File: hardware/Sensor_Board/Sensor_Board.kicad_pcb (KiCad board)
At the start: 4 copper layers, 83 x 83 mm, 67 parts, among them J1 Antenna, J2 Antenna, J3 Sensors, U1 ICM-42670-P, U10 PE42421, U12 SX1262IMLTRT, U2 SX1262IMLTRT, U3 0900FM15D0039, U4 BME280, U5 PE42421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

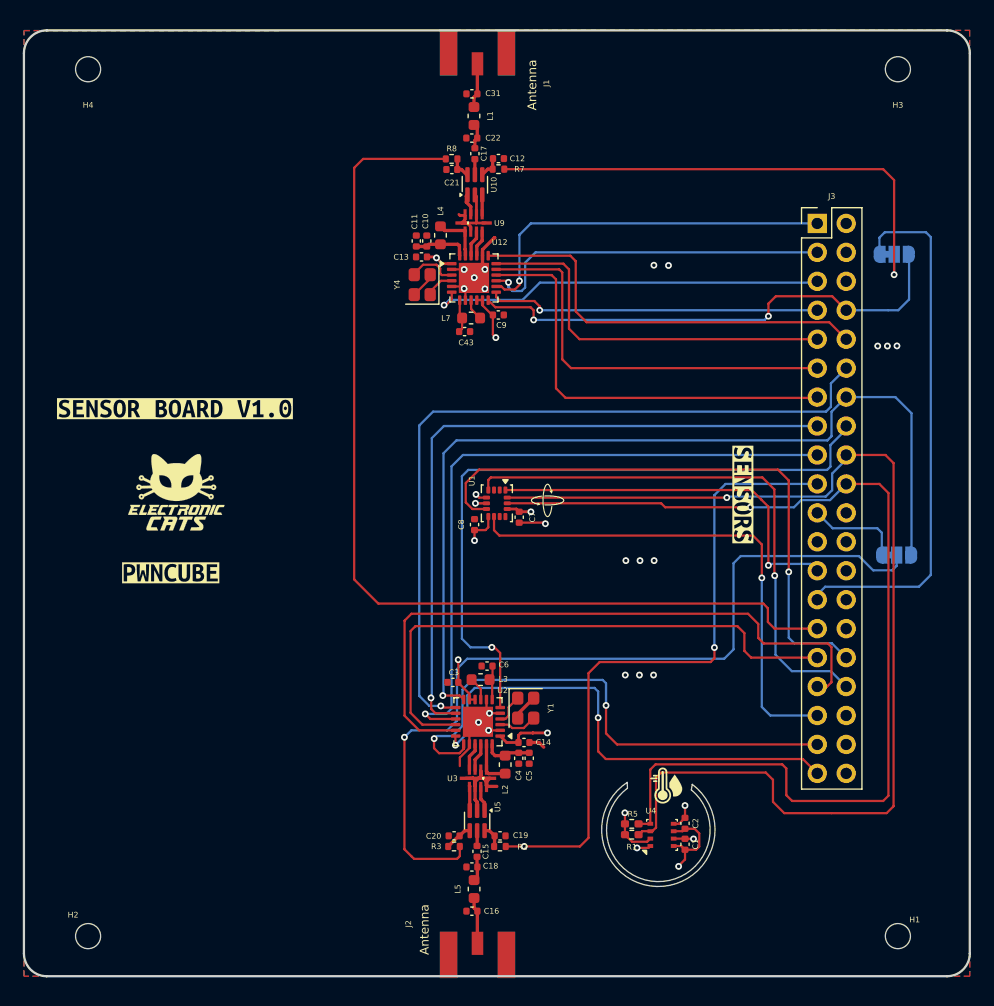
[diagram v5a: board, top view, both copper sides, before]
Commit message: feat(Hw):labels_updated
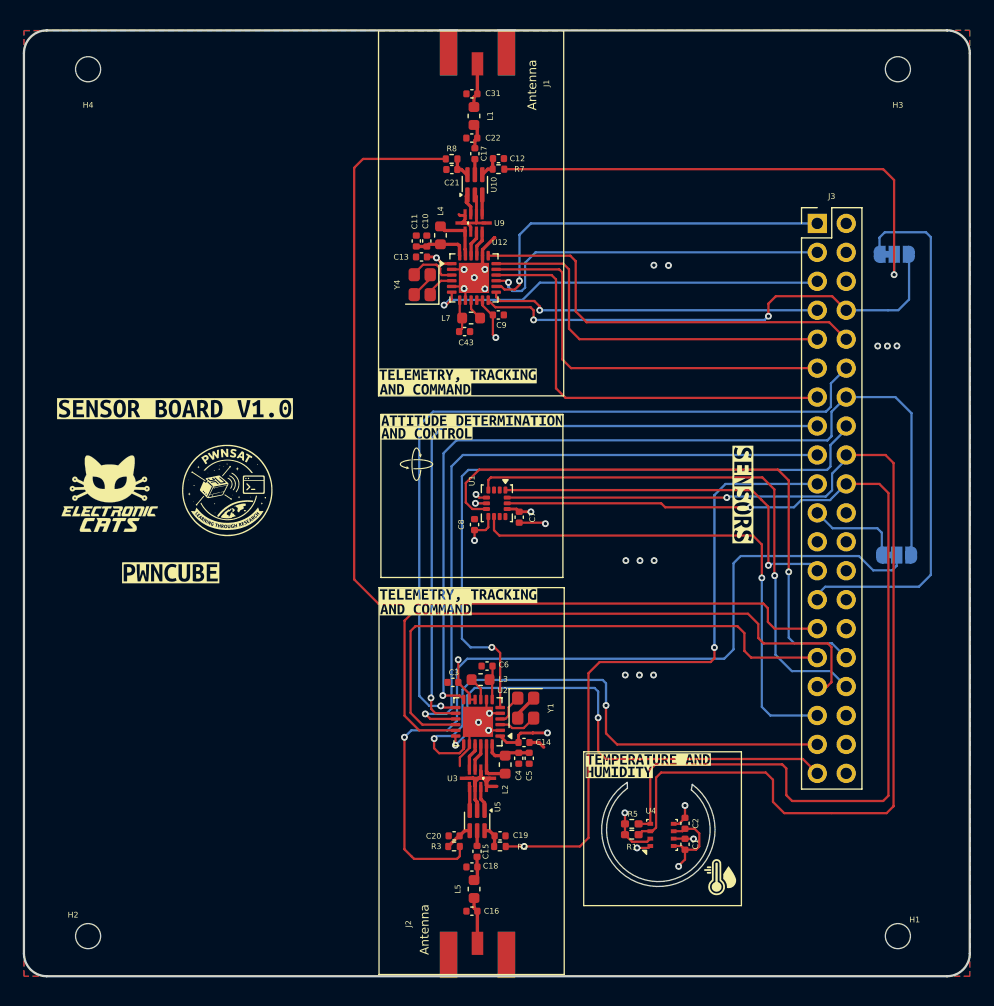
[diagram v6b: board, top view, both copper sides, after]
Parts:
- added kibuzzard-698668F8: G***, kibuzzard-698668F8, F.Cu at (124.6, 122.6)
- added kibuzzard-69866904: G***, kibuzzard-69866904, F.Cu at (122.0, 123.7)
- added kibuzzard-698669D4: G***, kibuzzard-698669D4, F.Cu at (107.9, 108.3)
- added kibuzzard-698669D4: G***, kibuzzard-698669D4, F.Cu at (107.9, 89.0)
- added kibuzzard-698669E3: G***, kibuzzard-698669E3, F.Cu at (105.0, 109.4)
- added kibuzzard-698669E3: G***, kibuzzard-698669E3, F.Cu at (105.0, 90.2)
- added kibuzzard-69866AEC: G***, kibuzzard-69866AEC, F.Cu at (109.1, 92.9)
- added kibuzzard-69866B09: G***, kibuzzard-69866B09, F.Cu at (105.1, 94.0)
- moved G*** 11.9 mm to (104.2, 96.7)
- moved G*** 9.33 mm to (130.9, 133.0)
- moved G*** 5.84 mm to (77.3, 99.3)

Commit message: feat(Hw):BoM´s_Updated
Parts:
- C10, C13, C14, C3, C4, C9: value 0.1uF -> 100nF
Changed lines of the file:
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@@
 				(font
 					(size 0.001 0.001)
+					(thickness 0.15)
 				)
 			)
@@
 				(font
 					(size 0.001 0.001)
+					(thickness 0.15)
 				)
 			)
@@
 				(font
 					(size 0.001 0.001)
+					(thickness 0.15)
 				)
 			)
@@
 				(font
 					(size 0.001 0.001)
+					(thickness 0.15)
 				)
 			)
@@
 			)
 		)
+		(property "LCSC#" "C170151"
+			(at 0 0 90)
+			(unlocked yes)
+			(layer "F.Fab")
+			(hide yes)
+			(effects
+				(font
+					(size 1 1)
+					(thickness 0.15)
+				)
+			)
+		)
 		(property ki_fp_filters "C_*")
 		(sheetname "/Sensors/")
@@
 			)
 		)
-		(property "LCSC#" "C710873 "
+		(property "LCSC#" "C76947"
 			(at 0 0 180)
 			(unlocked yes)
@@
 			)
 		)
-		(property "LCSC#" "C710873 "
+		(property "LCSC#" "C76947"
 			(at 0 0 0)
 			(unlocked yes)
@@
 			)
 		)
-		(property "Value" "0.1uF"
+		(property "Value" "100nF"
 			(at 0 1.16 0)
 			(layer "F.Fab")
@@
 			)
 		)
-		(property "Value" "0.1uF"
+		(property "Value" "100nF"
 			(at 0 1.16 90)
 			(layer "F.Fab")
@@
 			)
 		)
-		(property "Value" "0.1uF"
+		(property "Value" "100nF"
 			(at 0 1.16 90)
 			(layer "F.Fab")
@@
 				(font
 					(size 0.001 0.001)
+					(thickness 0.15)
 				)
 			)
@@
 				(font
 					(size 0.001 0.001)
+					(thickness 0.15)
 				)
 			)
@@
 				(font
 					(size 0.001 0.001)
+					(thickness 0.15)
 				)
 			)
@@
 				(font
 					(size 0.001 0.001)
+					(thickness 0.15)
 				)
 			)
@@
 			)
 		)
-		(property "Datasheet" "https://datasheet.lcsc.com/lcsc/2110081230_Sunlord-SDFL1608T150KTF_C57838.pdf"
+		(property "Datasheet" "https://www.lcsc.com/datasheet/C2885870.pdf"
 			(at 0 0 0)
 			(layer "F.Fab")
@@
 			)
 		)
-		(property "LCSC#" "C57838"
+		(property "LCSC#" "C2885870"
 			(at 0 0 180)
 			(unlocked yes)
@@
 			)
 		)
+		(property "LCSC#" "C7501249"
+			(at 0 0 0)
+			(unlocked yes)
+			(layer "F.Fab")
+			(hide yes)
+			(effects
+				(font
+					(size 1 1)
+					(thickness 0.15)
+				)
+			)
+		)
 		(property ki_fp_filters "Connector*:*_2x??_*")
 		(sheetname "/Inputs_Connectors/")
@@
 			)
 		)
-		(property "LCSC#" "C710873 "
+		(property "LCSC#" "C76947"
 			(at 0 0 0)
 			(unlocked yes)
@@
 			)
 		)
-		(property "Value" "0.1uF"
+		(property "Value" "100nF"
 			(at 0 1.16 0)
 			(layer "F.Fab")
@@
 			)
 		)
-		(property "Datasheet" "~"
+		(property "Datasheet" ""
 			(at 0 0 90)
 			(layer "F.Fab")
@@
 			)
 		)
-		(property "Datasheet" "~"
+		(property "Datasheet" ""
 			(at 0 0 90)
 			(layer "F.Fab")
@@
 				(font
 					(size 0.001 0.001)
+					(thickness 0.15)
 				)
 			)
@@
 				(font
 					(size 0.001 0.001)
+					(thickness 0.15)
 				)
 			)
@@
 			)
 		)
-		(property "Datasheet" "https://datasheet.lcsc.com/lcsc/2110081230_Sunlord-SDFL1608T150KTF_C57838.pdf"
+		(property "Datasheet" "https://www.lcsc.com/datasheet/C2885870.pdf"
 			(at 0 0 0)
 			(layer "F.Fab")
@@
 			)
 		)
-		(property "LCSC#" "C57838"
+		(property "LCSC#" "C2885870"
 			(at 0 0 0)
 			(unlocked yes)
@@
 			)
 		)
-		(property "Value" "0.1uF"
+		(property "Value" "100nF"
 			(at 0 1.16 0)
 			(layer "F.Fab")
@@
 			)
 		)
-		(property "LCSC#" "C710873 "
+		(property "LCSC#" "C76947"
 			(at 0 0 180)
 			(unlocked yes)
@@
 			)
 		)
-		(property "Datasheet" "~"
+		(property "Datasheet" ""
 			(at 0 0 90)
 			(layer "F.Fab")
@@
 				(font
 					(size 0.001 0.001)
+					(thickness 0.15)
 				)
 			)
@@
 				(font
 					(size 0.001 0.001)
+					(thickness 0.15)
 				)
 			)
@@
 			)
 		)
-		(property "Value" "0.1uF"
+		(property "Value" "100nF"
 			(at 0 1.16 0)
 			(layer "F.Fab")
